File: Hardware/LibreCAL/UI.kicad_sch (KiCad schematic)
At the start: 24 parts, among them SW2 TL3301CF160QG, SW3 TL3301CF160QG

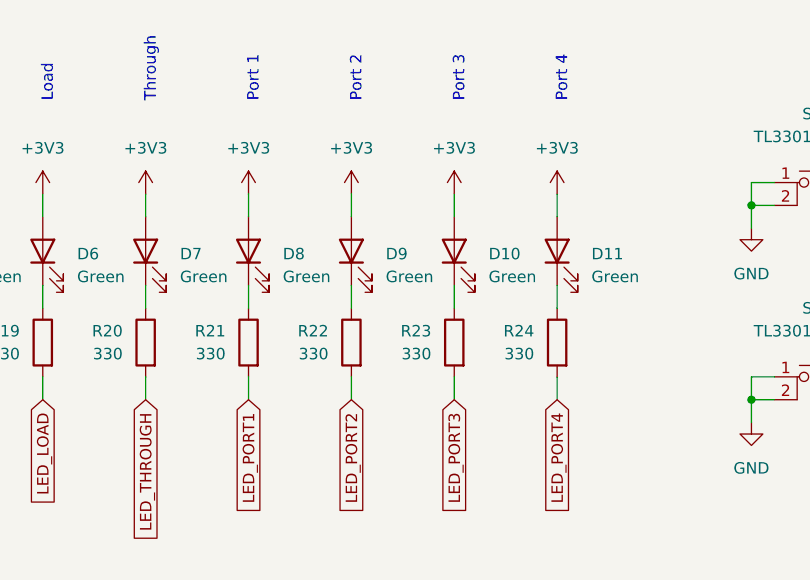
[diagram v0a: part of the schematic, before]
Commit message: Filters added, housing updated
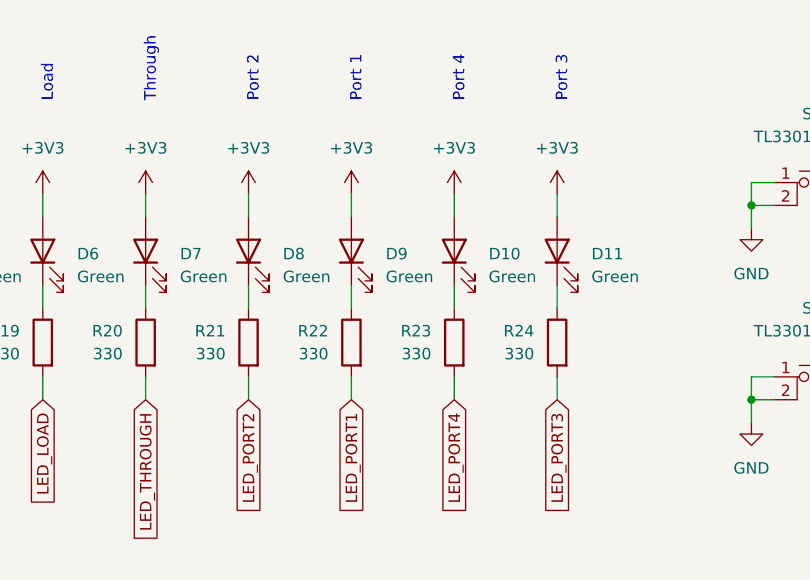
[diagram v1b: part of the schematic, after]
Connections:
- net LED_PORT1: now also R22.2; no longer R21.2
- net LED_PORT2: now also R21.2; no longer R22.2
- net LED_PORT3: now also R24.2; no longer R23.2
- net LED_PORT4: now also R23.2; no longer R24.2
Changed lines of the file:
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@@
     (effects (font (size 1.27 1.27)) (justify left bottom))
   )
-  (text "Port 4" (at 177.8 76.2 90)
+  (text "Port 3" (at 177.8 76.2 90)
     (effects (font (size 1.27 1.27)) (justify left bottom))
   )
@@
     (effects (font (size 1.27 1.27)) (justify left bottom))
   )
-  (text "Port 2" (at 154.94 76.2 90)
+  (text "Port 1" (at 154.94 76.2 90)
     (effects (font (size 1.27 1.27)) (justify left bottom))
   )
@@
     (effects (font (size 1.27 1.27)) (justify left bottom))
   )
-  (text "Port 1" (at 143.51 76.2 90)
+  (text "Port 2" (at 143.51 76.2 90)
     (effects (font (size 1.27 1.27)) (justify left bottom))
   )
@@
     (effects (font (size 1.27 1.27)) (justify left bottom))
   )
-  (text "Port 3" (at 166.37 76.2 90)
+  (text "Port 4" (at 166.37 76.2 90)
     (effects (font (size 1.27 1.27)) (justify left bottom))
   )
-  (global_label "LED_PORT3" (shape input) (at 165.1 109.22 270) (fields_autoplaced)
+  (global_label "LED_PORT4" (shape input) (at 165.1 109.22 270) (fields_autoplaced)
     (effects (font (size 1.27 1.27)) (justify right))
     (property "Intersheet References" "${INTERSHEET_REFS}" (id 0) (at 165.0206 122.0955 90)
@@
     )
   )
-  (global_label "LED_PORT4" (shape input) (at 176.53 109.22 270) (fields_autoplaced)
+  (global_label "LED_PORT3" (shape input) (at 176.53 109.22 270) (fields_autoplaced)
     (effects (font (size 1.27 1.27)) (justify right))
     (property "Intersheet References" "${INTERSHEET_REFS}" (id 0) (at 176.4506 122.0955 90)
@@
     )
   )
-  (global_label "LED_PORT1" (shape input) (at 142.24 109.22 270) (fields_autoplaced)
+  (global_label "LED_PORT2" (shape input) (at 142.24 109.22 270) (fields_autoplaced)
     (effects (font (size 1.27 1.27)) (justify right))
     (property "Intersheet References" "${INTERSHEET_REFS}" (id 0) (at 142.1606 122.0955 90)
@@
     )
   )
-  (global_label "LED_PORT2" (shape input) (at 153.67 109.22 270) (fields_autoplaced)
+  (global_label "LED_PORT1" (shape input) (at 153.67 109.22 270) (fields_autoplaced)
     (effects (font (size 1.27 1.27)) (justify right))
     (property "Intersheet References" "${INTERSHEET_REFS}" (id 0) (at 153.5906 122.0955 90)

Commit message: replaced bootsel switch, adjusted covers
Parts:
- SW2, SW3: footprint LibreCAL:TL3301-J -> LibreCAL:TL3301C-J
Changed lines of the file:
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@@
     (property "Reference" "SW2" (id 0) (at 205.74 77.47 0))
     (property "Value" "TL3301CF160QG" (id 1) (at 205.74 80.01 0))
-    (property "Footprint" "LibreCAL:TL3301-J" (id 2) (at 205.74 80.01 0)
+    (property "Footprint" "LibreCAL:TL3301C-J" (id 2) (at 205.74 80.01 0)
       (effects (font (size 1.27 1.27)) hide)
     )
@@
     (property "Reference" "SW3" (id 0) (at 205.74 99.06 0))
     (property "Value" "TL3301CF160QG" (id 1) (at 205.74 101.6 0))
-    (property "Footprint" "LibreCAL:TL3301-J" (id 2) (at 205.74 101.6 0)
+    (property "Footprint" "LibreCAL:TL3301C-J" (id 2) (at 205.74 101.6 0)
       (effects (font (size 1.27 1.27)) hide)
     )

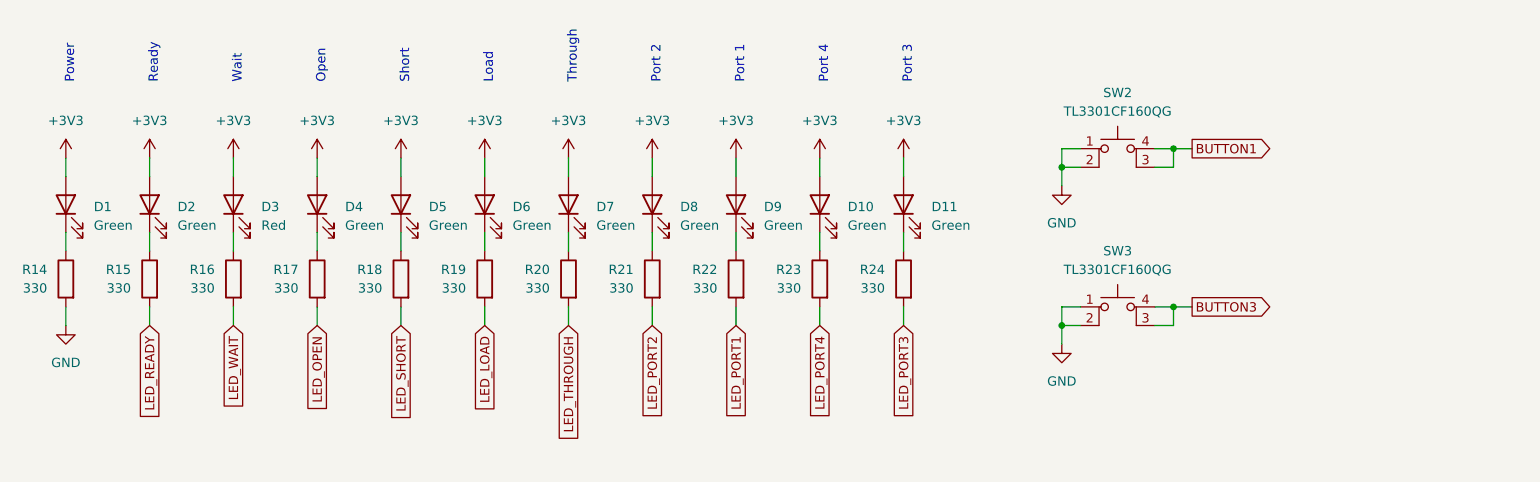
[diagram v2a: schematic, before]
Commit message: Improvements on LibreCAL KiCad: fixed minor errors/labels(cosmetic), improved BOM(Added LCSC_Part), improved Impedance JLCPCB 4Layer JLC7628 1.6mm
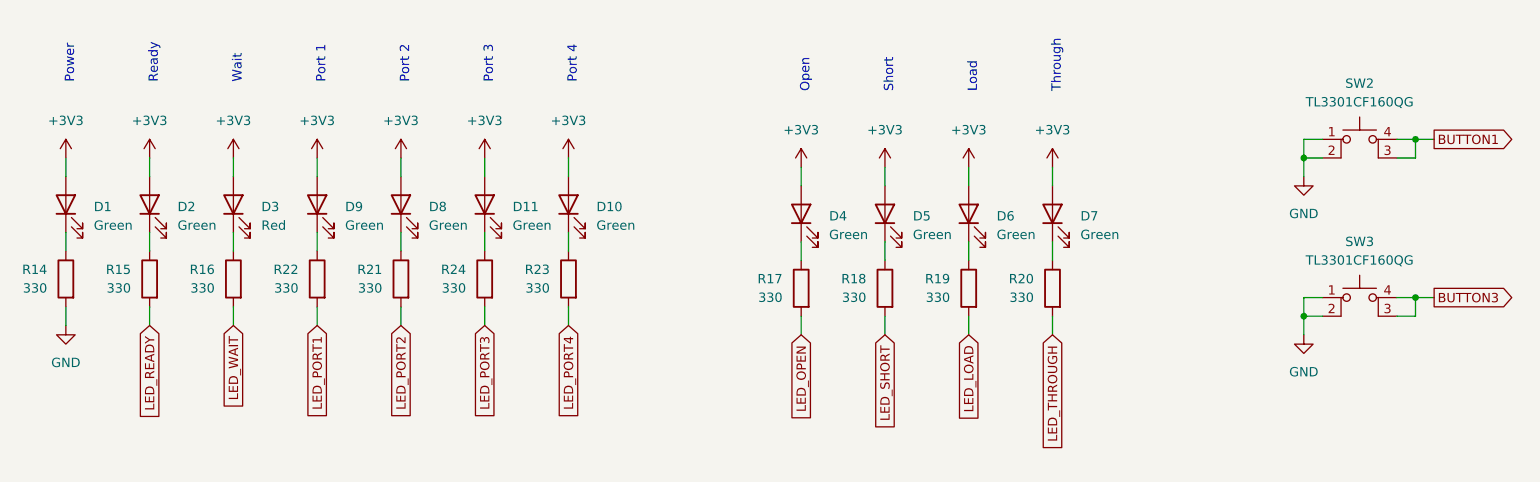
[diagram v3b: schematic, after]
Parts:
- D1, D10, D11, D2, D4, D5, D6, D7, D8, D9: LCSC_Part (none) -> C72043
- D3: LCSC_Part (none) -> C93128
- R14, R15, R16, R17, R18, R19, R20, R21, R22, R23, R24: LCSC_Part (none) -> C25104
- SW2, SW3: LCSC_Part (none) -> C273522
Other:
- title: (none) -> LibreCAL
- moved on the sheet: D10, D11, D4, D5, D6, D7, D8, D9, R17, R18, R19, R20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
